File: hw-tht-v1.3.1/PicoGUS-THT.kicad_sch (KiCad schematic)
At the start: 38 parts, among them J1 IRQDMA_JP, J3 Bus_ISA_8bit, J5 SJ1-3535NG, J6 UART_TX, J7 USB power jumper, U1 Pico, U10 74AHCT126, U2 74AHC244, U3 SN74CB3T3257, U4 SN74CB3T3257, U5 74AHC14, U6 74AHC00, U7 74AHC00, U8 APS6404L-3SQR-SN

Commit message: THT rev B: review fixes, C34 220uF, schematic PDF
Schematic
- C34 (USB VBUS bulk) 220 uF low-impedance Rubycon 16ZLH220MEFC6.3X11
  (USB 2.0 asks for >= 120 uF per host port)
- own UUID namespace for the rev B items (the USB sheet had reused UUIDs of
  v1.3.0 items, which mixed up ERC markers)
- TP1-TP3 pin names empty ("") in the embedded Pico_USB copy (KiCad 10 drew
  "~" literally)
- R25/R26 DigiKey/LCSC fields, U3/U4 adapter note (PA0034C first, BOB-13994
  has 0.635 mm pads), U12 in the title block's SMD list, USB sheet note
  reworded, USB-C always-on VBUS warning
- schematic PDF re-exported (4 pages)

Board
- U1: the library footprint's Pico pin-name/SWD silkscreen texts removed
  again (as in the v1.3.0 label clean-up)
- U3/U4 references back at their v1.3.0 spots (were on the gold fingers)
- U1, U3, U4 back in their footprint groups
- VBUS_USB in the pwr net class

BOM: C34 own line; BOM, uploads and socket BOM regenerated.

Co-Authored-By: Claude Opus 5.5 <noreply@anthropic.com>
Claude-Session: https://claude.ai/code/session_011utN3x8yYUNDvkpGCEq5yD
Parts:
- U3, U4: Alternatives 300-mil adapter: SparkFun BOB-13994 or Chip Quik PA0034C (D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 -> 300-mil adapter in the DIP pads: Chip Quik PA0034C (DK 315-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
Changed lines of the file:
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@@
 		(rev "v1.3.1")
 		(comment 1 "Through-hole variant of PicoGUS v1.2 with Waveblaster header; rev B: USB host port")
-		(comment 2 "SMD only: U8, U9; U3/U4 TSSOP-16 or a 300-mil DIP-16 adapter (nested footprint)")
+		(comment 2 "SMD only: U8, U9, U12 (optional ESD); U3/U4 TSSOP-16 or on a 300-mil DIP-16 adapter (nested footprint)")
 	)
 	(text "Saves PIO instructions due to JMP limitations"
@@
 			)
 		)
-		(property "Alternatives" "300-mil adapter: SparkFun BOB-13994 or Chip Quik PA0034C (DK 315-PA0034C-ND), optionally in a DIP-16 socket"
+		(property "Alternatives" "300-mil adapter in the DIP pads: Chip Quik PA0034C (DK 315-PA0034C-ND, round pins fitted) or SparkFun BOB-13994 (0.635 mm pads: align the 0.65 mm TSSOP carefully), optionally in a DIP-16 socket"
 			(at 69.215 123.19 0)
 			(hide yes)
@@
 			)
 		)
-		(property "Alternatives" "300-mil adapter: SparkFun BOB-13994 or Chip Quik PA0034C (DK 315-PA0034C-ND), optionally in a DIP-16 socket"
+		(property "Alternatives" "300-mil adapter in the DIP pads: Chip Quik PA0034C (DK 315-PA0034C-ND, round pins fitted) or SparkFun BOB-13994 (0.635 mm pads: align the 0.65 mm TSSOP carefully), optionally in a DIP-16 socket"
 			(at 25.4 123.19 0)
 			(hide yes)

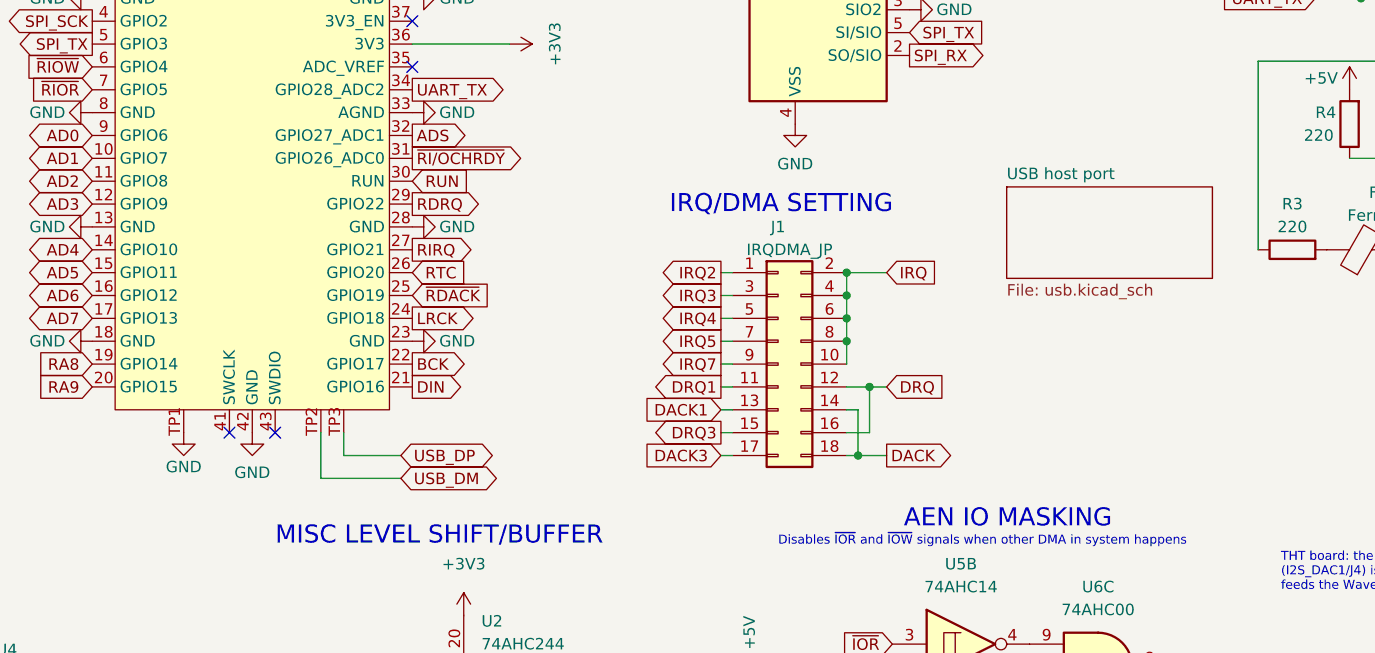
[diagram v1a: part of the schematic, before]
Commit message: THT rev B: user's new placement; USB port and Waveblaster standoff holes dropped
- PicoGUS-THT.kicad_pcb: the user's rev B placement (Pico moved down, bracket
  parts and mixer regrouped), unrouted
- USB host port removed again (usb.kicad_sch, J11, F1, C34, C35, U12); U1 back
  on the v1.3.0 Pico symbol and RPi_Pico_SMD_TH footprint
- J9 on the new Wavetable_NoMountingHoles footprint (no daughterboard standoff
  holes; the far one landed in U4); standoff and screws dropped from the BOM
- card outline: the 6.35 mm Edge.Cuts step at x 197.41 next to the ISA
  fingers had been dragged off the board in the upload; restored
- design rules identical to v1.3.0
- BOM, DigiKey uploads, socket BOM, schematic PDF and README updated

Co-Authored-By: Claude Opus 5.5 <noreply@anthropic.com>
Claude-Session: https://claude.ai/code/session_011utN3x8yYUNDvkpGCEq5yD
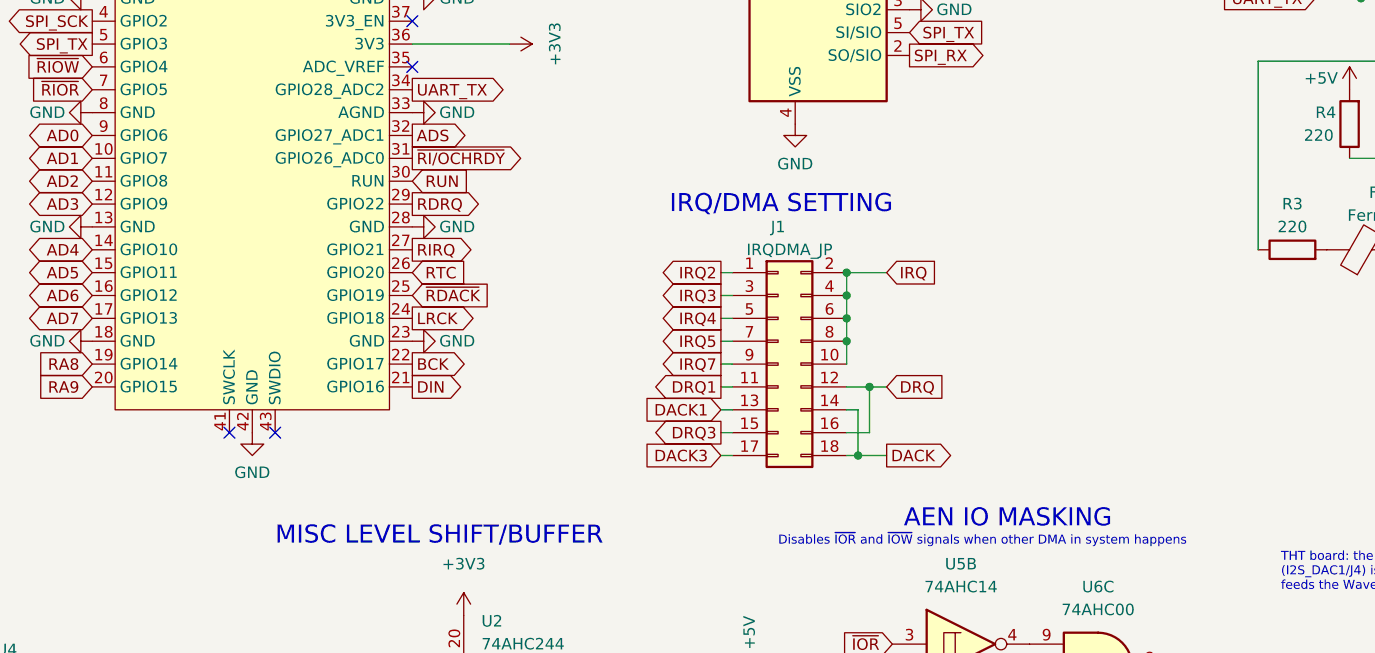
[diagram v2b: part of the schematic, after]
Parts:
- U1: footprint PiGUS library:RPi_Pico_SMD_TH_USB -> PiGUS library:RPi_Pico_SMD_TH; symbol PiGUS library:Pico_USB -> PiGUS library:Pico
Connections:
- net GND: no longer U1.TP1
- removed net USB_DM: U1.TP2
- removed net USB_DP: U1.TP3
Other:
- removed sheet USB host port
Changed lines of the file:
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@@
 		(date "2026-10-18")
 		(rev "v1.3.1")
-		(comment 1 "Through-hole variant of PicoGUS v1.2 with Waveblaster header; rev B: USB host port")
-		(comment 2 "SMD only: U8, U9, U12 (optional ESD); U3/U4 TSSOP-16 or on a 300-mil DIP-16 adapter (nested footprint)")
+		(comment 1 "Through-hole variant of PicoGUS v1.2 with Waveblaster header; rev B: new placement")
+		(comment 2 "SMD only: U8, U9; U3/U4 TSSOP-16 or on a 300-mil DIP-16 adapter (nested footprint)")
 	)
 	(text "Saves PIO instructions due to JMP limitations"
@@
 	)
 	(symbol
-		(lib_id "PiGUS library:Pico_USB")
+		(lib_id "PiGUS library:Pico")
 		(at 109.22 61.595 0)
 		(unit 1)
@@
 			)
 		)
-		(property "Footprint" "PiGUS library:RPi_Pico_SMD_TH_USB"
+		(property "Footprint" "PiGUS library:RPi_Pico_SMD_TH"
 			(at 109.22 61.595 90)
 			(hide yes)
@@
 			)
 		)
-		(property "Description" "Raspberry Pi Pico (or Pico H) on 2x20 headers; soldered flat (no headers) for the USB port: its test points TP1-TP3 are soldered from the back"
+		(property "Description" "Raspberry Pi Pico (or Pico H) on 2x20 headers"
 			(at 109.22 61.595 0)
 			(hide yes)
@@
 		(pin "9"
 		)
-		(pin "TP1"
-		)
-		(pin "TP2"
-		)
-		(pin "TP3"
-		)
 		(instances
 			(project "PicoGUS-THT"
@@
 				)
 			)
-		)
-	)
-	(symbol
-		(lib_id "power:GND")
-		(at 101.6 90.805 0)
-		(unit 1)
-		(body_style 1)
-		(exclude_from_sim no)
-		(in_bom no)
-		(on_board yes)
-		(in_pos_files no)
-		(dnp no)
-		(property "Reference" "#PWR0199"
-			(at 101.6 97.155 0)
-			(hide yes)
-			(show_name no)
-			(do_not_autoplace no)
-			(effects
-				(font
-					(size 1.27 1.27)
-				)
-			)
-		)
-		(property "Value" "GND"
-			(at 101.6 94.615 0)
-			(show_name no)
-			(do_not_autoplace no)
-			(effects
-				(font
-					(size 1.27 1.27)
-				)
-			)
-		)
-		(property "Footprint" ""
-			(at 101.6 90.805 0)
-			(hide yes)
-			(show_name no)
-			(do_not_autoplace no)
-			(effects
-				(font
-					(size 1.27 1.27)
-				)
-			)
-		)
-		(property "Datasheet" ""
-			(at 101.6 90.805 0)
-			(hide yes)
-			(show_name no)
-			(do_not_autoplace no)
-			(effects
-				(font
-					(size 1.27 1.27)
-				)
-			)
-		)
-		(property "Description" ""
-			(at 101.6 90.805 0)
-			(hide yes)
-			(show_name no)
-			(do_not_autoplace no)
-			(effects
-				(font
-					(size 1.27 1.27)
-				)
-			)
-		)
-		(pin "1"
-		)
-		(instances
-			(project "PicoGUS-THT"
-				(path "/8fb4b197-630e-4faa-9892-8ecaeb71c13b"
-					(reference "#PWR0199")
-					(unit 1)
-				)
-			)
-		)
-	)
-	(wire
-		(pts
-			(xy 119.38 90.805)
-			(xy 119.38 93.345)
-		)
-		(stroke
-			(width 0)
-			(type default)
-		)
-	)
-	(wire
-		(pts
-			(xy 119.38 93.345)
-			(xy 125.73 93.345)
-		)
-		(stroke
-			(width 0)
-			(type default)
-		)
-	)
-	(wire
-		(pts
-			(xy 116.84 90.805)
-			(xy 116.84 95.885)
-		)
-		(stroke
-			(width 0)
-			(type default)
-		)
-	)
-	(wire
-		(pts
-			(xy 116.84 95.885)
-			(xy 125.73 95.885)
-		)
-		(stroke
-			(width 0)
-			(type default)
-		)
-	)
-	(global_label "USB_DP"
-		(shape bidirectional)
-		(at 125.73 93.345 0)
-		(fields_autoplaced yes)
-		(effects
-			(font
-				(size 1.27 1.27)
-			)
-			(justify left)
-		)
-		(property "Intersheetrefs" "${INTERSHEET_REFS}"
-			(at 125.73 93.345 0)
-			(hide yes)
-			(show_name no)
-			(do_not_autoplace no)
-			(effects
-				(font
-					(size 1.27 1.27)
-				)
-				(justify left)
-			)
-		)
-	)
-	(global_label "USB_DM"
-		(shape bidirectional)
-		(at 125.73 95.885 0)
-		(fields_autoplaced yes)
-		(effects
-			(font
-				(size 1.27 1.27)
-			)
-			(justify left)
-		)
-		(property "Intersheetrefs" "${INTERSHEET_REFS}"
-			(at 125.73 95.885 0)
-			(hide yes)
-			(show_name no)
-			(do_not_autoplace no)
-			(effects
-				(font
-					(size 1.27 1.27)
-				)
-				(justify left)
-			)
-		)
-	)
-	(sheet
-		(at 193.04 63.5)
-		(size 22.86 10.16)
-		(exclude_from_sim no)
-		(in_bom yes)
-		(on_board yes)
-		(dnp no)
-		(fields_autoplaced yes)
-		(stroke
-			(width 0.1524)
-			(type solid)
-		)
-		(fill
-			(color 0 0 0 0)
-		)
-		(property "Sheetname" "USB host port"
-			(at 193.04 62.7884 0)
-			(show_name no)
-			(do_not_autoplace no)
-			(effects
-				(font
-					(size 1.27 1.27)
-				)
-				(justify left bottom)
-			)
-		)
-		(property "Sheetfile" "usb.kicad_sch"
-			(at 193.04 74.2446 0)
-			(show_name no)
-			(do_not_autoplace no)
-			(effects
-				(font
-					(size 1.27 1.27)
-				)
-				(justify left top)
-			)
-		)
-		(instances
-			(project "PicoGUS-THT"
-				(path "/8fb4b197-630e-4faa-9892-8ecaeb71c13b"
-					(page "4")
-				)
-			)

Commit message: THT rev B: take 2 placement with the USB-A port back; C31 above U11
- PicoGUS-THT.kicad_pcb: the user's take-2 placement (USB-A J11 at the
  bracket, Pico lower, RV1/J8/J5/J11 down the bracket, U3/U4 upright),
  unrouted; J9 on Wavetable_NoMountingHoles; C31 moved to (177, 40.5) above
  U11 (was inside its DIP body); the dragged Edge.Cuts step at x 197.41
  restored again
- schematic: USB host port sheet and the Pico with USB test points back,
  J9 without standoff holes; VBUS_USB in the pwr net class
- BOM, DigiKey uploads, socket BOM, schematic PDF and README for the USB-A
  version (Pico soldered flat, no daughterboard standoff)

Co-Authored-By: Claude Opus 5.5 <noreply@anthropic.com>
Claude-Session: https://claude.ai/code/session_011utN3x8yYUNDvkpGCEq5yD
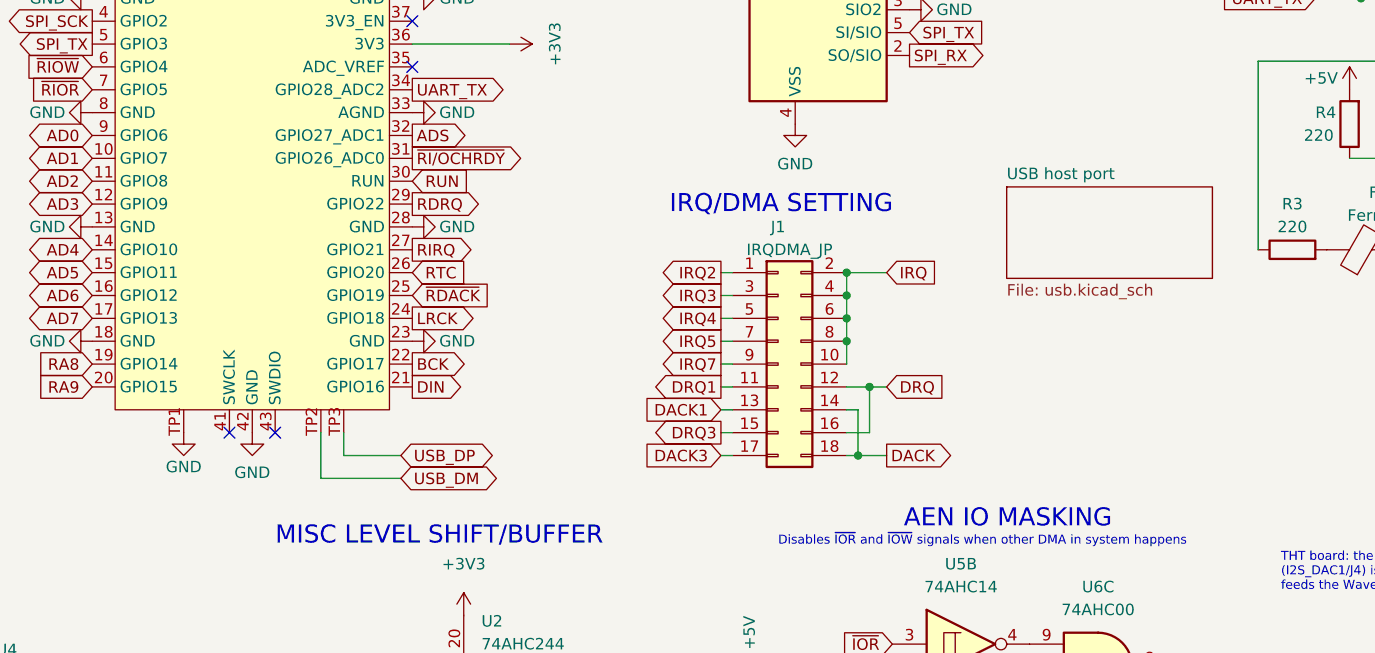
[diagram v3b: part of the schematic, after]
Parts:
- U1: footprint PiGUS library:RPi_Pico_SMD_TH -> PiGUS library:RPi_Pico_SMD_TH_USB; symbol PiGUS library:Pico -> PiGUS library:Pico_USB
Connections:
- net GND: now also U1.TP1
- new net USB_DM: U1.TP2
- new net USB_DP: U1.TP3
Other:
- added sheet USB host port (usb.kicad_sch)
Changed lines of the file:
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@@
 		(date "2026-10-18")
 		(rev "v1.3.1")
-		(comment 1 "Through-hole variant of PicoGUS v1.2 with Waveblaster header; rev B: new placement")
-		(comment 2 "SMD only: U8, U9; U3/U4 TSSOP-16 or on a 300-mil DIP-16 adapter (nested footprint)")
+		(comment 1 "Through-hole variant of PicoGUS v1.2 with Waveblaster header; rev B: USB host port")
+		(comment 2 "SMD only: U8, U9, U12 (optional ESD); U3/U4 TSSOP-16 or on a 300-mil DIP-16 adapter (nested footprint)")
 	)
 	(text "Saves PIO instructions due to JMP limitations"
@@
 	)
 	(symbol
-		(lib_id "PiGUS library:Pico")
+		(lib_id "PiGUS library:Pico_USB")
 		(at 109.22 61.595 0)
 		(unit 1)
@@
 			)
 		)
-		(property "Footprint" "PiGUS library:RPi_Pico_SMD_TH"
+		(property "Footprint" "PiGUS library:RPi_Pico_SMD_TH_USB"
 			(at 109.22 61.595 90)
 			(hide yes)
@@
 			)
 		)
-		(property "Description" "Raspberry Pi Pico (or Pico H) on 2x20 headers"
+		(property "Description" "Raspberry Pi Pico (or Pico H) on 2x20 headers; soldered flat (no headers) for the USB port: its test points TP1-TP3 are soldered from the back"
 			(at 109.22 61.595 0)
 			(hide yes)
@@
 		(pin "9"
 		)
+		(pin "TP1"
+		)
+		(pin "TP2"
+		)
+		(pin "TP3"
+		)
 		(instances
 			(project "PicoGUS-THT"
@@
 				)
 			)
+		)
+	)
+	(symbol
+		(lib_id "power:GND")
+		(at 101.6 90.805 0)
+		(unit 1)
+		(body_style 1)
+		(exclude_from_sim no)
+		(in_bom no)
+		(on_board yes)
+		(in_pos_files no)
+		(dnp no)
+		(property "Reference" "#PWR0199"
+			(at 101.6 97.155 0)
+			(hide yes)
+			(show_name no)
+			(do_not_autoplace no)
+			(effects
+				(font
+					(size 1.27 1.27)
+				)
+			)
+		)
+		(property "Value" "GND"
+			(at 101.6 94.615 0)
+			(show_name no)
+			(do_not_autoplace no)
+			(effects
+				(font
+					(size 1.27 1.27)
+				)
+			)
+		)
+		(property "Footprint" ""
+			(at 101.6 90.805 0)
+			(hide yes)
+			(show_name no)
+			(do_not_autoplace no)
+			(effects
+				(font
+					(size 1.27 1.27)
+				)
+			)
+		)
+		(property "Datasheet" ""
+			(at 101.6 90.805 0)
+			(hide yes)
+			(show_name no)
+			(do_not_autoplace no)
+			(effects
+				(font
+					(size 1.27 1.27)
+				)
+			)
+		)
+		(property "Description" ""
+			(at 101.6 90.805 0)
+			(hide yes)
+			(show_name no)
+			(do_not_autoplace no)
+			(effects
+				(font
+					(size 1.27 1.27)
+				)
+			)
+		)
+		(pin "1"
+		)
+		(instances
+			(project "PicoGUS-THT"
+				(path "/8fb4b197-630e-4faa-9892-8ecaeb71c13b"
+					(reference "#PWR0199")
+					(unit 1)
+				)
+			)
+		)
+	)
+	(wire
+		(pts
+			(xy 119.38 90.805)
+			(xy 119.38 93.345)
+		)
+		(stroke
+			(width 0)
+			(type default)
+		)
+	)
+	(wire
+		(pts
+			(xy 119.38 93.345)
+			(xy 125.73 93.345)
+		)
+		(stroke
+			(width 0)
+			(type default)
+		)
+	)
+	(wire
+		(pts
+			(xy 116.84 90.805)
+			(xy 116.84 95.885)
+		)
+		(stroke
+			(width 0)
+			(type default)
+		)
+	)
+	(wire
+		(pts
+			(xy 116.84 95.885)
+			(xy 125.73 95.885)
+		)
+		(stroke
+			(width 0)
+			(type default)
+		)
+	)
+	(global_label "USB_DP"
+		(shape bidirectional)
+		(at 125.73 93.345 0)
+		(fields_autoplaced yes)
+		(effects
+			(font
+				(size 1.27 1.27)
+			)
+			(justify left)
+		)
+		(property "Intersheetrefs" "${INTERSHEET_REFS}"
+			(at 125.73 93.345 0)
+			(hide yes)
+			(show_name no)
+			(do_not_autoplace no)
+			(effects
+				(font
+					(size 1.27 1.27)
+				)
+				(justify left)
+			)
+		)
+	)
+	(global_label "USB_DM"
+		(shape bidirectional)
+		(at 125.73 95.885 0)
+		(fields_autoplaced yes)
+		(effects
+			(font
+				(size 1.27 1.27)
+			)
+			(justify left)
+		)
+		(property "Intersheetrefs" "${INTERSHEET_REFS}"
+			(at 125.73 95.885 0)
+			(hide yes)
+			(show_name no)
+			(do_not_autoplace no)
+			(effects
+				(font
+					(size 1.27 1.27)
+				)
+				(justify left)
+			)
+		)
+	)
+	(sheet
+		(at 193.04 63.5)
+		(size 22.86 10.16)
+		(exclude_from_sim no)
+		(in_bom yes)
+		(on_board yes)
+		(dnp no)
+		(fields_autoplaced yes)
+		(stroke
+			(width 0.1524)
+			(type solid)
+		)
+		(fill
+			(color 0 0 0 0)
+		)
+		(property "Sheetname" "USB host port"
+			(at 193.04 62.7884 0)
+			(show_name no)
+			(do_not_autoplace no)
+			(effects
+				(font
+					(size 1.27 1.27)
+				)
+				(justify left bottom)
+			)
+		)
+		(property "Sheetfile" "usb.kicad_sch"
+			(at 193.04 74.2446 0)
+			(show_name no)
+			(do_not_autoplace no)
+			(effects
+				(font
+					(size 1.27 1.27)
+				)
+				(justify left top)
+			)
+		)
+		(instances
+			(project "PicoGUS-THT"
+				(path "/8fb4b197-630e-4faa-9892-8ecaeb71c13b"
+					(page "4")
+				)
+			)

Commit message: THT rev B: U3/U4 back to the v1.3.0 TSSOP-16 footprint (DIP-16 option dropped)
Schematic: U3/U4 footprint, description and fields as on v1.3.0; title note updated. BOM: U3/U4 line
back to SMD only, the DIP-16 socket and TSSOP-to-DIP adapter lines removed (main and socket BOM,
DigiKey uploads). README: the nested-footprint option and its socket notes removed.

The board still has the nested footprints; the re-placed and re-routed board follows.

Co-Authored-By: Claude Opus 5.5 <noreply@anthropic.com>
Claude-Session: https://claude.ai/code/session_011utN3x8yYUNDvkpGCEq5yD
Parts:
- U3, U4: footprint PiGUS library:DIP-16_W7.62mm_TSSOP-16_Nested -> Package_SO:TSSOP-16_4.4x5mm_P0.65mm; Alternatives 300-mil adapter in the DIP pads: Chip Quik PA0034C (DK 315-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 -> (none)
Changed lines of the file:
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@@
 		(rev "v1.3.1")
 		(comment 1 "Through-hole variant of PicoGUS v1.2 with Waveblaster header; rev B: USB host port")
-		(comment 2 "SMD only: U8, U9, U12 (optional ESD); U3/U4 TSSOP-16 or on a 300-mil DIP-16 adapter (nested footprint)")
+		(comment 2 "Through-hole parts only; U3/U4, U8, U9 and U12 (optional ESD) exist in SMD only")
 	)
 	(text "Saves PIO instructions due to JMP limitations"
@@
 			)
 		)
-		(property "Footprint" "PiGUS library:DIP-16_W7.62mm_TSSOP-16_Nested"
+		(property "Footprint" "Package_SO:TSSOP-16_4.4x5mm_P0.65mm"
 			(at 90.805 120.65 0)
 			(hide yes)
@@
 			)
 		)
-		(property "Description" "FET mux w/ 5V->3V3 level shift. TSSOP-16 soldered directly, or on a 300-mil TSSOP-16 to DIP-16 adapter in the DIP pads"
+		(property "Description" "FET mux w/ 5V->3V3 level shift. SMD only"
 			(at 90.805 125.73 0)
 			(hide yes)
@@
 			)
 		)
-		(property "Alternatives" "300-mil adapter in the DIP pads: Chip Quik PA0034C (DK 315-PA0034C-ND, round pins fitted) or SparkFun BOB-13994 (0.635 mm pads: align the 0.65 mm TSSOP carefully), optionally in a DIP-16 socket"
-			(at 69.215 123.19 0)
-			(hide yes)
-			(effects
-				(font
-					(size 1.27 1.27)
-				)
-				(hide yes)
-			)
-		)
 		(pin "1"
 		)
@@
 			)
 		)
-		(property "Footprint" "PiGUS library:DIP-16_W7.62mm_TSSOP-16_Nested"
+		(property "Footprint" "Package_SO:TSSOP-16_4.4x5mm_P0.65mm"
 			(at 46.99 120.65 0)
 			(hide yes)
@@
 			)
 		)
-		(property "Description" "FET mux w/ 5V->3V3 level shift. TSSOP-16 soldered directly, or on a 300-mil TSSOP-16 to DIP-16 adapter in the DIP pads"
+		(property "Description" "FET mux w/ 5V->3V3 level shift. SMD only"
 			(at 46.99 125.73 0)
 			(hide yes)
@@
 			(at 25.4 123.19 0)
 			(hide yes)
-			(effects
-				(font
-					(size 1.27 1.27)
-				)
-				(hide yes)
-			)
-		)
-		(property "Alternatives" "300-mil adapter in the DIP pads: Chip Quik PA0034C (DK 315-PA0034C-ND, round pins fitted) or SparkFun BOB-13994 (0.635 mm pads: align the 0.65 mm TSSOP carefully), optionally in a DIP-16 socket"
-			(at 25.4 123.19 0)
-			(hide yes)
